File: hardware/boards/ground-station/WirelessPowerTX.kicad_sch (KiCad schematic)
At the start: 30 parts, among them U5 BQ501210RGCT

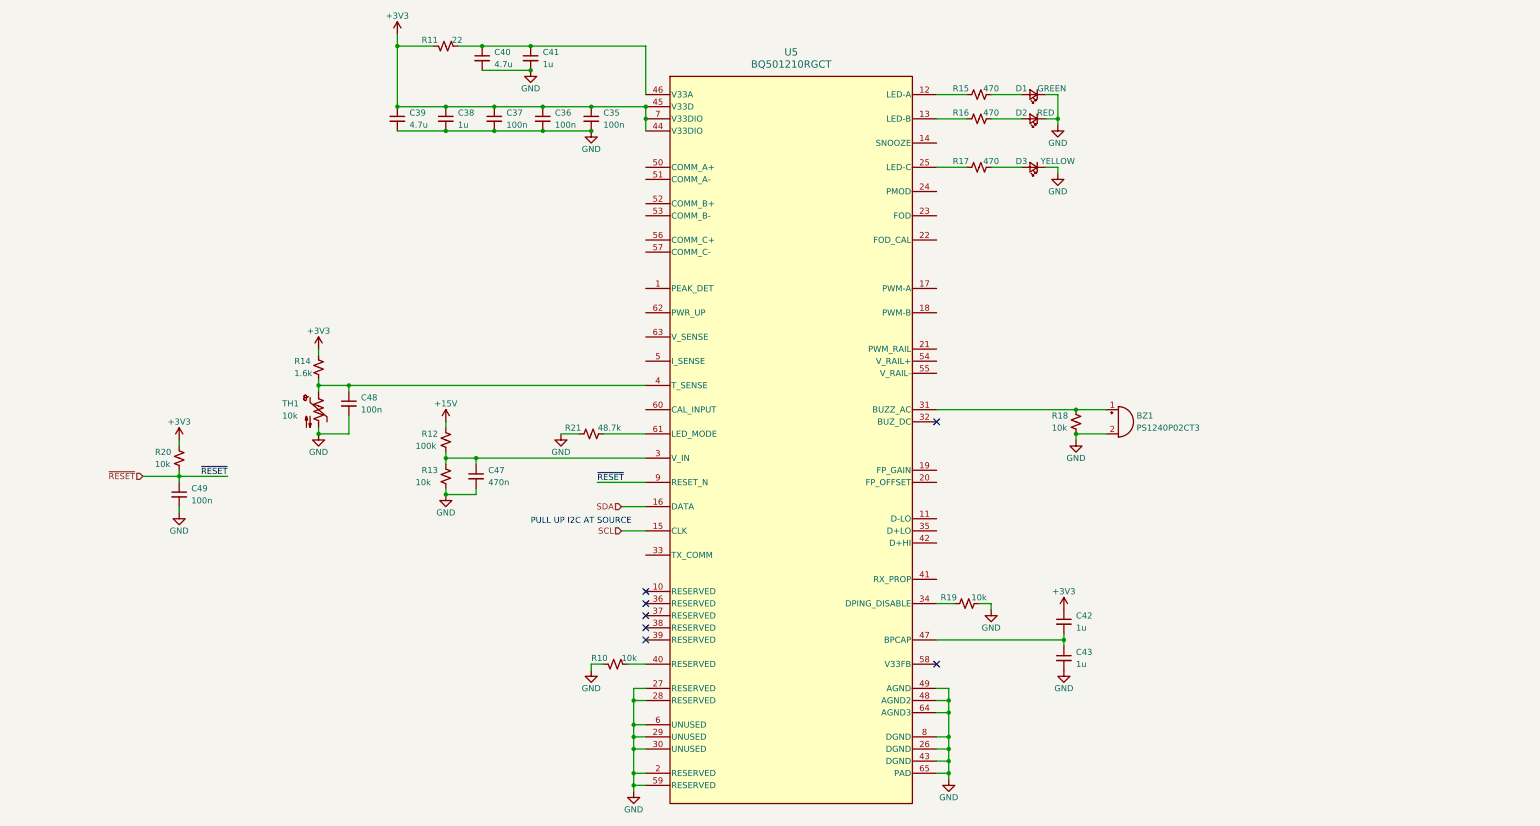
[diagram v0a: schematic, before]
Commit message: Transmitting power (without wires) (wire delete)
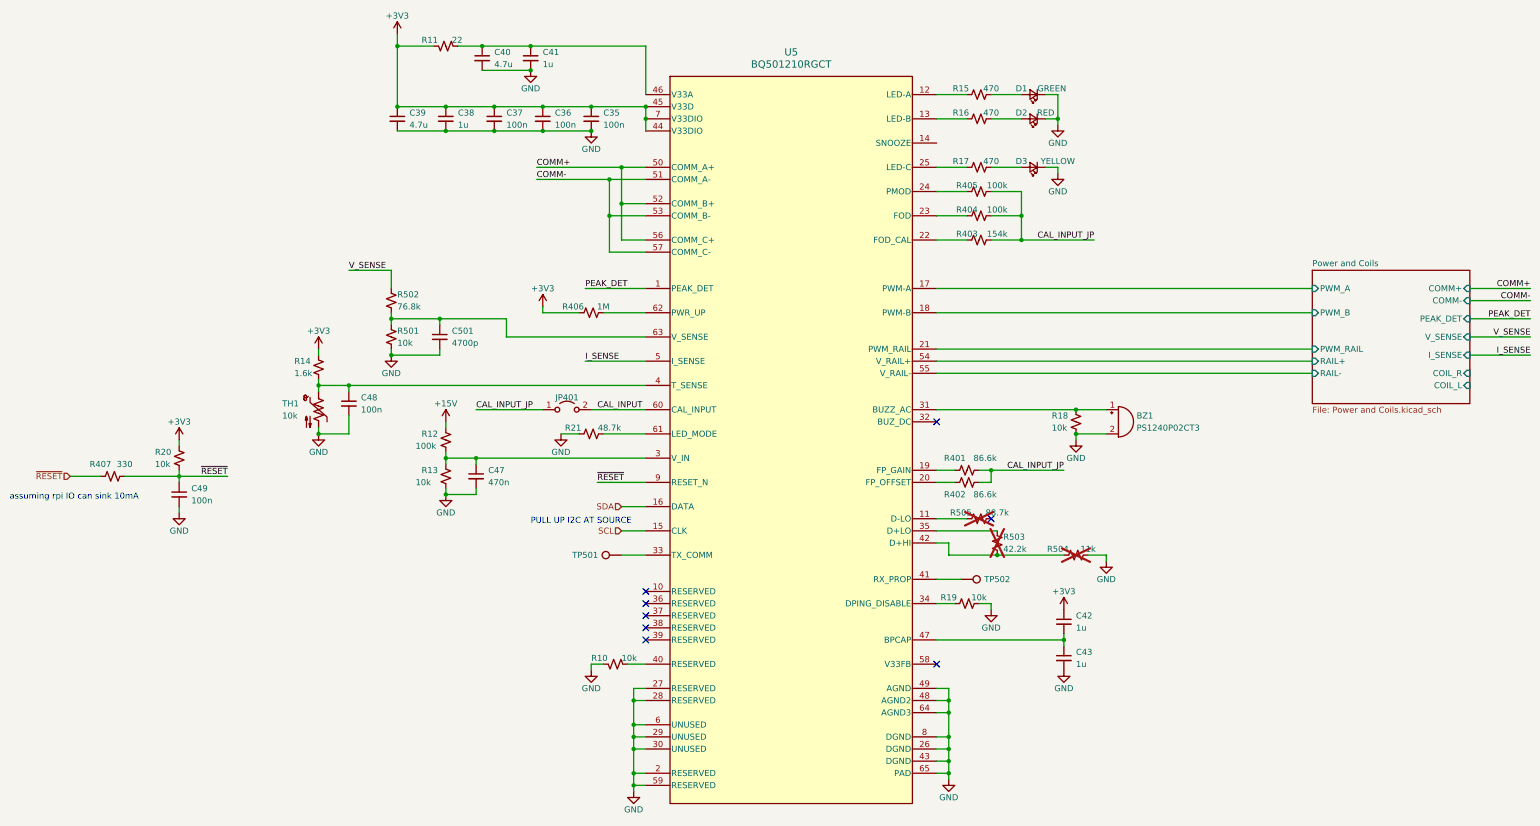
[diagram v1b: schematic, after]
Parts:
- added C501: 4700p, symbol Device:C_Small
- added JP401: Jumper_2_Open, symbol Jumper:Jumper_2_Open
- added R401, R402: 86.6k, symbol Device:R_Small_US
- added R403: 154k, symbol Device:R_Small_US
- added R404, R405: 100k, symbol Device:R_Small_US
- added R406: 1M, symbol Device:R_Small_US
- added R407: 330, symbol Device:R_Small_US
- added R501: 10k, symbol Device:R_Small_US
- added R502: 76.8k, symbol Device:R_Small_US
- added R503: 42.2k, symbol Device:R_Small_US
- added R504: 11k, symbol Device:R_Small_US
- added R505: 88.7k, symbol Device:R_Small_US
- added TP501, TP502: TestPoint, symbol Connector:TestPoint
- U5: Ref Design (none) -> https://www.ti.com/lit/ug/slvuao6/slvuao6.pdf?ts=1703886705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
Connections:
- net +3V3: now also R406.1
- net GND: now also C501.2, R501.2, R504.2
- net ~{RESET}: now also R407.1, R407.2
- net PEAK_DET: now reaches U5.1 (PEAK_DET)
- net at U5.11 (D-LO): now also R505.1
- net Power and Coils/PWM_A: now reaches U5.17 (PWM-A)
- net Power and Coils/PWM_B: now reaches U5.18 (PWM-B)
- net at U5.19 (FP_GAIN): now also R401.1
- net at U5.20 (FP_OFFSET): now also R402.1
- net Power and Coils/PWM_RAIL: now reaches U5.21 (PWM_RAIL)
- net at U5.22 (FOD_CAL): now also R403.1
- net at U5.23 (FOD): now also R404.1
- net at U5.24 (PMOD): now also R405.1
- net at U5.33 (TX_COMM): now also TP501.1
- net at U5.35 (D+LO): now also R503.1
- net at U5.41 (RX_PROP): now also TP502.1
- net at U5.42 (D+HI): now also R503.2, R504.1
- net I_SENSE: now reaches U5.5 (I_SENSE)
- net COMM+: now reaches U5.50 (COMM_A+)
- net COMM+: now also U5.52 (COMM_B+), U5.56 (COMM_C+)
- net COMM-: now reaches U5.51 (COMM_A-)
- net COMM-: now also U5.53 (COMM_B-), U5.57 (COMM_C-)
- net Power and Coils/RAIL+: now reaches U5.54 (V_RAIL+)
- net Power and Coils/RAIL-: now reaches U5.55 (V_RAIL-)
- net CAL_INPUT: now reaches U5.60 (CAL_INPUT)
- net CAL_INPUT: now also JP401.2 (B)
- net at U5.62 (PWR_UP): now also R406.2
- net at U5.63 (V_SENSE): now also C501.1, R501.1, R502.2
- new net CAL_INPUT_JP: JP401.1 (A), R401.2, R402.2, R403.2, R404.2, R405.2
- new net V_SENSE: R502.1
- no-connect marks 7 -> 8
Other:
- added sheet Power and Coils (Power and Coils.kicad_sch)
- note added: "assuming rpi IO can sink 10mA"
